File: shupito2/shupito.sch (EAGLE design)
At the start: 88 parts, among them IC2 74LVC1T45, IC3 74LVC1T45, IC4 74LVC1T45, IC5 74LVC1T45, IC6 ATXMEGA32A4U-AU, IC7 TPS73033DBV, Q1 BC807W-1907646, Q10 1758094, Q11 PDTC123YU-1757992, Q2 NX2301P-1894738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

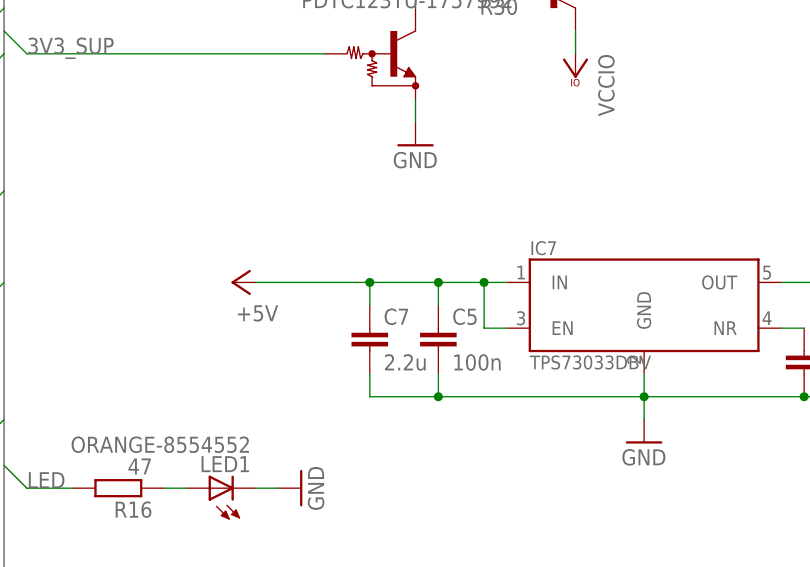
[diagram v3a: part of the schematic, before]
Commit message: Added a protection diode for the 3.3v ldo.
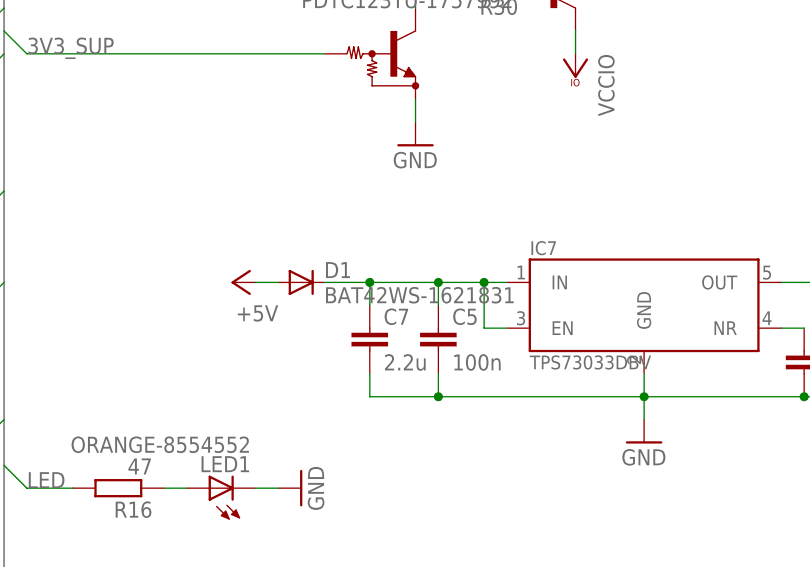
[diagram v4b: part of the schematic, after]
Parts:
- added D1: BAT42WS-1621831, diode:DIODE-SOD323
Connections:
- new net N$13: C5.1, C7.1, D1.C, IC7.EN, IC7.IN
- net +5V: now also D1.A; no longer C5.1, C7.1, IC7.EN, IC7.IN
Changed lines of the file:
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@@
 <grid distance="0.1" unitdist="inch" unit="inch" style="lines" multiple="1" display="no" altdistance="0.01" altunitdist="inch" altunit="inch"/>
 <layers>
-<layer number="1" name="Top" color="4" fill="1" visible="yes" active="no"/>
-<layer number="16" name="Bottom" color="1" fill="1" visible="yes" active="no"/>
-<layer number="17" name="Pads" color="2" fill="1" visible="yes" active="no"/>
-<layer number="18" name="Vias" color="2" fill="1" visible="yes" active="no"/>
-<layer number="19" name="Unrouted" color="6" fill="1" visible="yes" active="no"/>
-<layer number="20" name="Dimension" color="15" fill="1" visible="yes" active="no"/>
-<layer number="21" name="tPlace" color="7" fill="1" visible="yes" active="no"/>
-<layer number="22" name="bPlace" color="7" fill="1" visible="yes" active="no"/>
-<layer number="23" name="tOrigins" color="15" fill="1" visible="yes" active="no"/>
-<layer number="24" name="bOrigins" color="15" fill="1" visible="yes" active="no"/>
-<layer number="25" name="tNames" color="7" fill="1" visible="yes" active="no"/>
-<layer number="26" name="bNames" color="7" fill="1" visible="yes" active="no"/>
-<layer number="27" name="tValues" color="7" fill="1" visible="yes" active="no"/>
-<layer number="28" name="bValues" color="7" fill="1" visible="yes" active="no"/>
+<layer number="1" name="Top" color="4" fill="1" visible="no" active="no"/>
+<layer number="16" name="Bottom" color="1" fill="1" visible="no" active="no"/>
+<layer number="17" name="Pads" color="2" fill="1" visible="no" active="no"/>
+<layer number="18" name="Vias" color="2" fill="1" visible="no" active="no"/>
+<layer number="19" name="Unrouted" color="6" fill="1" visible="no" active="no"/>
+<layer number="20" name="Dimension" color="15" fill="1" visible="no" active="no"/>
+<layer number="21" name="tPlace" color="7" fill="1" visible="no" active="no"/>
+<layer number="22" name="bPlace" color="7" fill="1" visible="no" active="no"/>
+<layer number="23" name="tOrigins" color="15" fill="1" visible="no" active="no"/>
+<layer number="24" name="bOrigins" color="15" fill="1" visible="no" active="no"/>
+<layer number="25" name="tNames" color="7" fill="1" visible="no" active="no"/>
+<layer number="26" name="bNames" color="7" fill="1" visible="no" active="no"/>
+<layer number="27" name="tValues" color="7" fill="1" visible="no" active="no"/>
+<layer number="28" name="bValues" color="7" fill="1" visible="no" active="no"/>
 <layer number="29" name="tStop" color="7" fill="3" visible="no" active="no"/>
 <layer number="30" name="bStop" color="7" fill="6" visible="no" active="no"/>
@@
 <layer number="35" name="tGlue" color="7" fill="4" visible="no" active="no"/>
 <layer number="36" name="bGlue" color="7" fill="5" visible="no" active="no"/>
-<layer number="37" name="tTest" color="7" fill="1" visible="yes" active="no"/>
-<layer number="38" name="bTest" color="7" fill="1" visible="yes" active="no"/>
+<layer number="37" name="tTest" color="7" fill="1" visible="no" active="no"/>
+<layer number="38" name="bTest" color="7" fill="1" visible="no" active="no"/>
 <layer number="39" name="tKeepout" color="4" fill="11" visible="no" active="no"/>
 <layer number="40" name="bKeepout" color="1" fill="11" visible="no" active="no"/>
@@
 <layer number="44" name="Drills" color="7" fill="1" visible="no" active="no"/>
 <layer number="45" name="Holes" color="7" fill="1" visible="no" active="no"/>
-<layer number="46" name="Milling" color="3" fill="1" visible="yes" active="no"/>
-<layer number="47" name="Measures" color="7" fill="1" visible="yes" active="no"/>
-<layer number="48" name="Document" color="7" fill="1" visible="yes" active="no"/>
-<layer number="49" name="Reference" color="7" fill="1" visible="yes" active="no"/>
-<layer number="50" name="dxf" color="7" fill="1" visible="yes" active="no"/>
-<layer number="51" name="tDocu" color="7" fill="1" visible="yes" active="no"/>
-<layer number="52" name="bDocu" color="7" fill="1" visible="yes" active="no"/>
+<layer number="46" name="Milling" color="3" fill="1" visible="no" active="no"/>
+<layer number="47" name="Measures" color="7" fill="1" visible="no" active="no"/>
+<layer number="48" name="Document" color="7" fill="1" visible="no" active="no"/>
+<layer number="49" name="Reference" color="7" fill="1" visible="no" active="no"/>
+<layer number="50" name="dxf" color="7" fill="1" visible="no" active="no"/>
+<layer number="51" name="tDocu" color="7" fill="1" visible="no" active="no"/>
+<layer number="52" name="bDocu" color="7" fill="1" visible="no" active="no"/>
 <layer number="91" name="Nets" color="2" fill="1" visible="yes" active="yes"/>
 <layer number="92" name="Busses" color="1" fill="1" visible="yes" active="yes"/>
@@
 <attribute name="TP_SIGNAL_NAME" value=""/>
 </part>
+<part name="D1" library="diode" deviceset="DIODE" device="-SOD323" value="BAT42WS-1621831"/>
 </parts>
 <sheets>
@@
 <instance part="R4" gate="G$1" x="58.42" y="297.18" rot="R180"/>
 <instance part="TP5" gate="G$1" x="17.78" y="101.6"/>
+<instance part="D1" gate="1" x="180.34" y="279.4"/>
 </instances>
 <busses>
@@
 </segment>
 <segment>
-<wire x1="200.66" y1="279.4" x2="203.2" y2="279.4" width="0.1524" layer="91"/>
-<wire x1="203.2" y1="274.32" x2="200.66" y2="274.32" width="0.1524" layer="91"/>
-<wire x1="200.66" y1="274.32" x2="200.66" y2="279.4" width="0.1524" layer="91"/>
-<wire x1="195.58" y1="279.4" x2="200.66" y2="279.4" width="0.1524" layer="91"/>
-<wire x1="195.58" y1="279.4" x2="195.58" y2="276.86" width="0.1524" layer="91"/>
-<wire x1="187.96" y1="279.4" x2="195.58" y2="279.4" width="0.1524" layer="91"/>
-<wire x1="187.96" y1="279.4" x2="187.96" y2="276.86" width="0.1524" layer="91"/>
-<wire x1="175.26" y1="279.4" x2="187.96" y2="279.4" width="0.1524" layer="91"/>
-<junction x="200.66" y="279.4"/>
-<junction x="195.58" y="279.4"/>
-<junction x="187.96" y="279.4"/>
-<pinref part="C7" gate="G$1" pin="1"/>
-<pinref part="C5" gate="G$1" pin="1"/>
-<pinref part="IC7" gate="G$1" pin="IN"/>
-<pinref part="IC7" gate="G$1" pin="EN"/>
-<pinref part="P+5" gate="1" pin="+5V"/>
-</segment>
-<segment>
 <wire x1="251.46" y1="27.94" x2="256.54" y2="27.94" width="0.1524" layer="91"/>
 <wire x1="256.54" y1="27.94" x2="259.08" y2="27.94" width="0.1524" layer="91"/>
@@
 <wire x1="114.3" y1="297.18" x2="132.08" y2="297.18" width="0.1524" layer="91"/>
 <junction x="114.3" y="297.18"/>
+</segment>
+<segment>
+<pinref part="P+5" gate="1" pin="+5V"/>
+<pinref part="D1" gate="1" pin="A"/>
+<wire x1="175.26" y1="279.4" x2="177.8" y2="279.4" width="0.1524" layer="91"/>
 </segment>
 </net>
@@
 </segment>
 </net>
+<net name="N$13" class="0">
+<segment>
+<wire x1="200.66" y1="279.4" x2="203.2" y2="279.4" width="0.1524" layer="91"/>
+<wire x1="203.2" y1="274.32" x2="200.66" y2="274.32" width="0.1524" layer="91"/>
+<wire x1="200.66" y1="274.32" x2="200.66" y2="279.4" width="0.1524" layer="91"/>
+<wire x1="195.58" y1="279.4" x2="200.66" y2="279.4" width="0.1524" layer="91"/>
+<wire x1="195.58" y1="279.4" x2="195.58" y2="276.86" width="0.1524" layer="91"/>
+<wire x1="187.96" y1="279.4" x2="195.58" y2="279.4" width="0.1524" layer="91"/>
+<wire x1="187.96" y1="279.4" x2="187.96" y2="276.86" width="0.1524" layer="91"/>
+<junction x="200.66" y="279.4"/>
+<junction x="195.58" y="279.4"/>
+<pinref part="C7" gate="G$1" pin="1"/>
+<pinref part="C5" gate="G$1" pin="1"/>
+<pinref part="IC7" gate="G$1" pin="IN"/>
+<pinref part="IC7" gate="G$1" pin="EN"/>
+<pinref part="D1" gate="1" pin="C"/>
+<wire x1="182.88" y1="279.4" x2="187.96" y2="279.4" width="0.1524" layer="91"/>
+<junction x="187.96" y="279.4"/>
+</segment>
+</net>

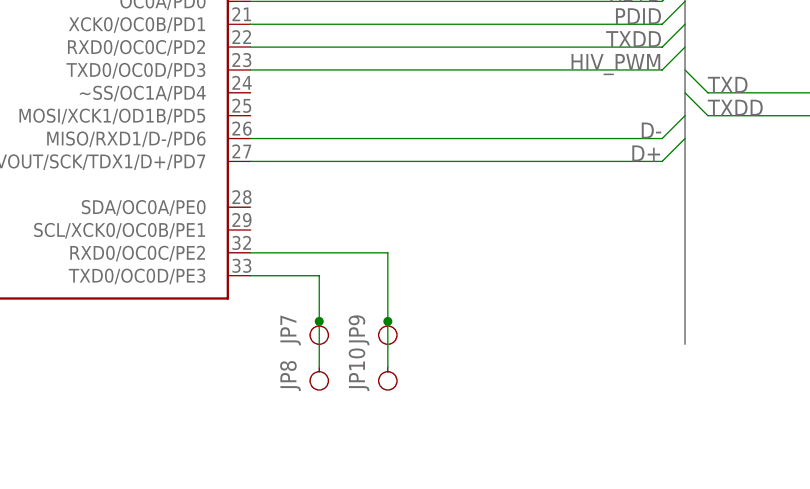
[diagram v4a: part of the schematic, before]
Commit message: Added GND and VCC to AUX connector.
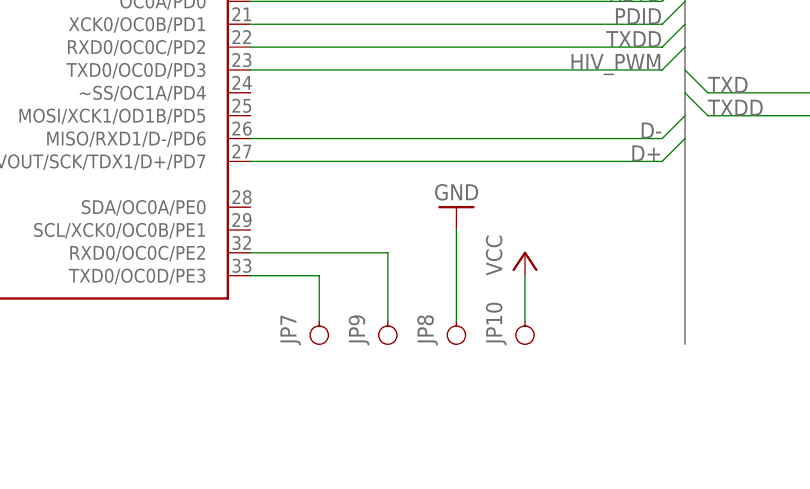
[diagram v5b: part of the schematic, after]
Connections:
- net GND: now also JP8.1
- net N$1: no longer JP8.1
- net N$12: no longer JP10.1
- net VCC: now also JP10.1
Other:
- moved on the sheet: JP10, JP8
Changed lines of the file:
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@@
 </part>
 <part name="D1" library="diode" deviceset="DIODE" device="-SOD323" value="BAT42WS-1621831"/>
+<part name="GND15" library="supply1" deviceset="GND" device=""/>
+<part name="P+10" library="supply1" deviceset="VCC" device=""/>
 </parts>
 <sheets>
@@
 <instance part="GND3" gate="1" x="127" y="325.12" rot="MR180"/>
 <instance part="JP7" gate="G$1" x="106.68" y="25.4" rot="R90"/>
-<instance part="JP8" gate="G$1" x="106.68" y="20.32" rot="R90"/>
+<instance part="JP8" gate="G$1" x="121.92" y="25.4" rot="R90"/>
 <instance part="JP9" gate="G$1" x="114.3" y="25.4" rot="R90"/>
-<instance part="JP10" gate="G$1" x="114.3" y="20.32" rot="R90"/>
+<instance part="JP10" gate="G$1" x="129.54" y="25.4" rot="R90"/>
 <instance part="C3" gate="G$1" x="114.3" y="294.64"/>
 <instance part="S1" gate="G$1" x="106.68" y="162.56"/>
@@
 <instance part="TP5" gate="G$1" x="17.78" y="101.6"/>
 <instance part="D1" gate="1" x="180.34" y="279.4"/>
+<instance part="GND15" gate="1" x="121.92" y="40.64" rot="R180"/>
+<instance part="P+10" gate="VCC" x="129.54" y="35.56"/>
 </instances>
 <busses>
@@
 <wire x1="17.78" y1="99.06" x2="17.78" y2="96.52" width="0.1524" layer="91"/>
 <junction x="17.78" y="96.52"/>
+</segment>
+<segment>
+<pinref part="P+10" gate="VCC" pin="VCC"/>
+<pinref part="JP10" gate="G$1" pin="1"/>
+<wire x1="129.54" y1="33.02" x2="129.54" y2="27.94" width="0.1524" layer="91"/>
 </segment>
 </net>
@@
 <pinref part="GND7" gate="1" pin="GND"/>
 </segment>
+<segment>
+<pinref part="GND15" gate="1" pin="GND"/>
+<pinref part="JP8" gate="G$1" pin="1"/>
+<wire x1="121.92" y1="38.1" x2="121.92" y2="27.94" width="0.1524" layer="91"/>
+</segment>
 </net>
 <net name="N$2" class="0">
@@
 <wire x1="99.06" y1="33.02" x2="106.68" y2="33.02" width="0.1524" layer="91"/>
 <wire x1="106.68" y1="33.02" x2="106.68" y2="27.94" width="0.1524" layer="91"/>
-<pinref part="JP8" gate="G$1" pin="1"/>
-<wire x1="106.68" y1="27.94" x2="106.68" y2="22.86" width="0.1524" layer="91"/>
-<junction x="106.68" y="27.94"/>
 </segment>
 </net>
@@
 <wire x1="99.06" y1="35.56" x2="114.3" y2="35.56" width="0.1524" layer="91"/>
 <wire x1="114.3" y1="35.56" x2="114.3" y2="27.94" width="0.1524" layer="91"/>
-<pinref part="JP10" gate="G$1" pin="1"/>
-<wire x1="114.3" y1="27.94" x2="114.3" y2="22.86" width="0.1524" layer="91"/>
-<junction x="114.3" y="27.94"/>
-</segment>
-</net>
+</segment>
+</net>
